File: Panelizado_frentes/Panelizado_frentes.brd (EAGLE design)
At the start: 130 x 100 mm, 17 parts, among them J2 F0504-H-05-10G-R, Q4 BSS138, Q5 BSS138, Q6 BSS138

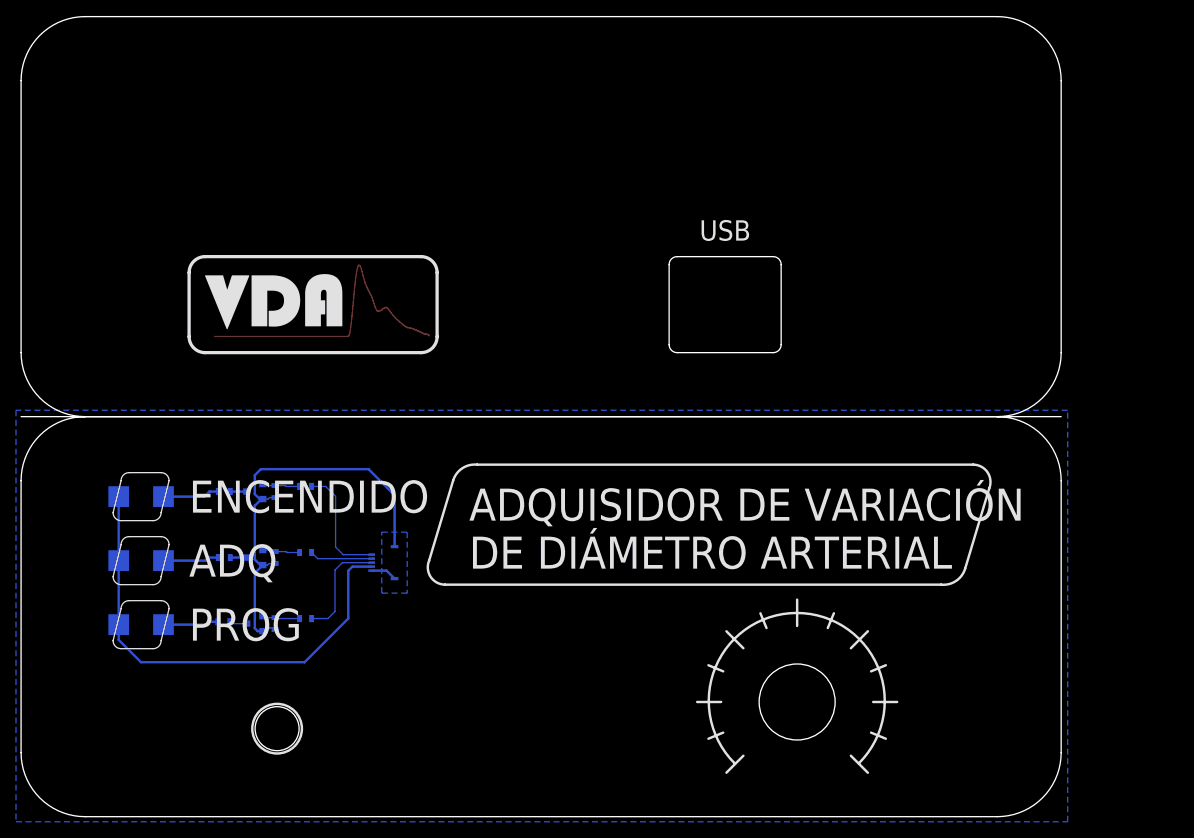
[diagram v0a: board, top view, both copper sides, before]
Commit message: BOM del adquisidor listo
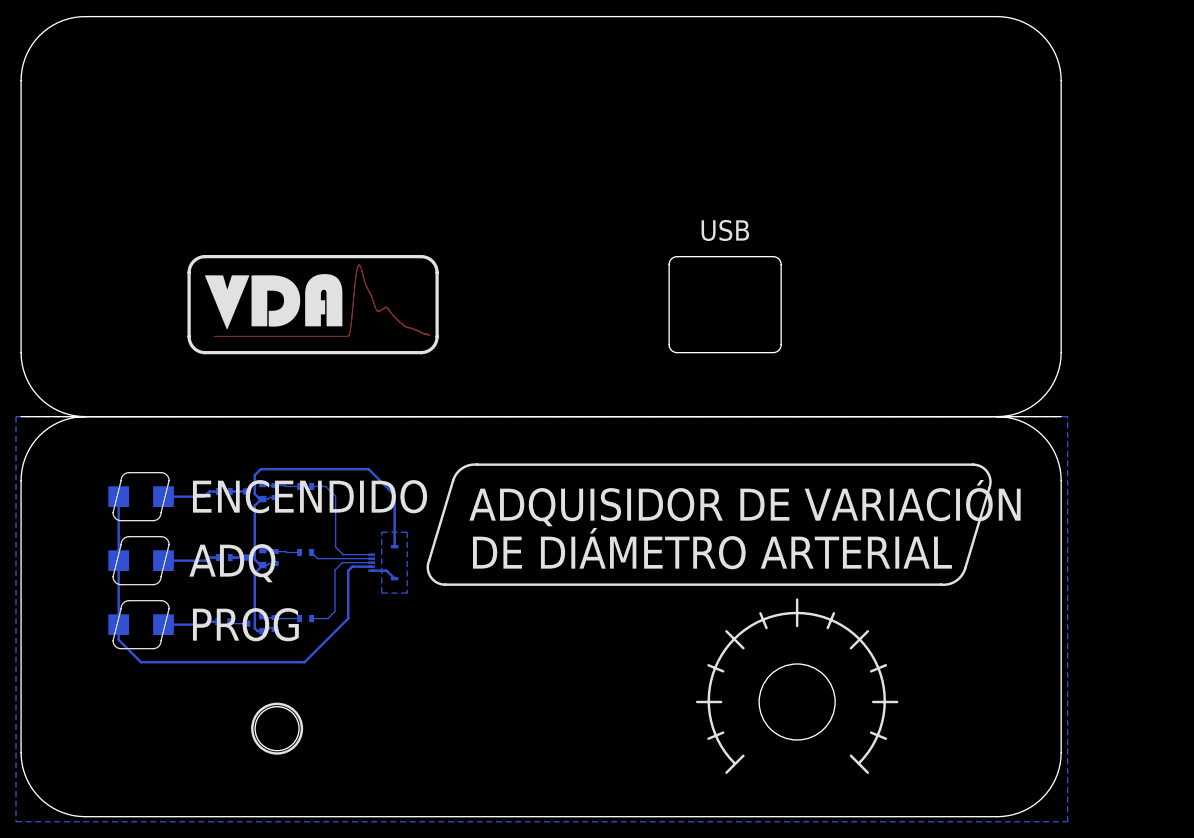
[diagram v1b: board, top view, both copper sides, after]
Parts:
- renumbered J2 to J1, Q4 to Q1, Q5 to Q2, Q6 to Q3, R10 to R2, R11 to R1, R12 to R5, R13 to R4, R14 to R8, R15 to R7, R16 to R3, R17 to R6, R18 to R9
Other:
- board text added: "WayWayWay"
